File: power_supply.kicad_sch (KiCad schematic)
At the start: 29 parts, among them CON1 USB_B_Micro, CON2 Barrel_Jack_MountingPin, Q1 AO3401A, U1 AP6503, U2 CP2102N

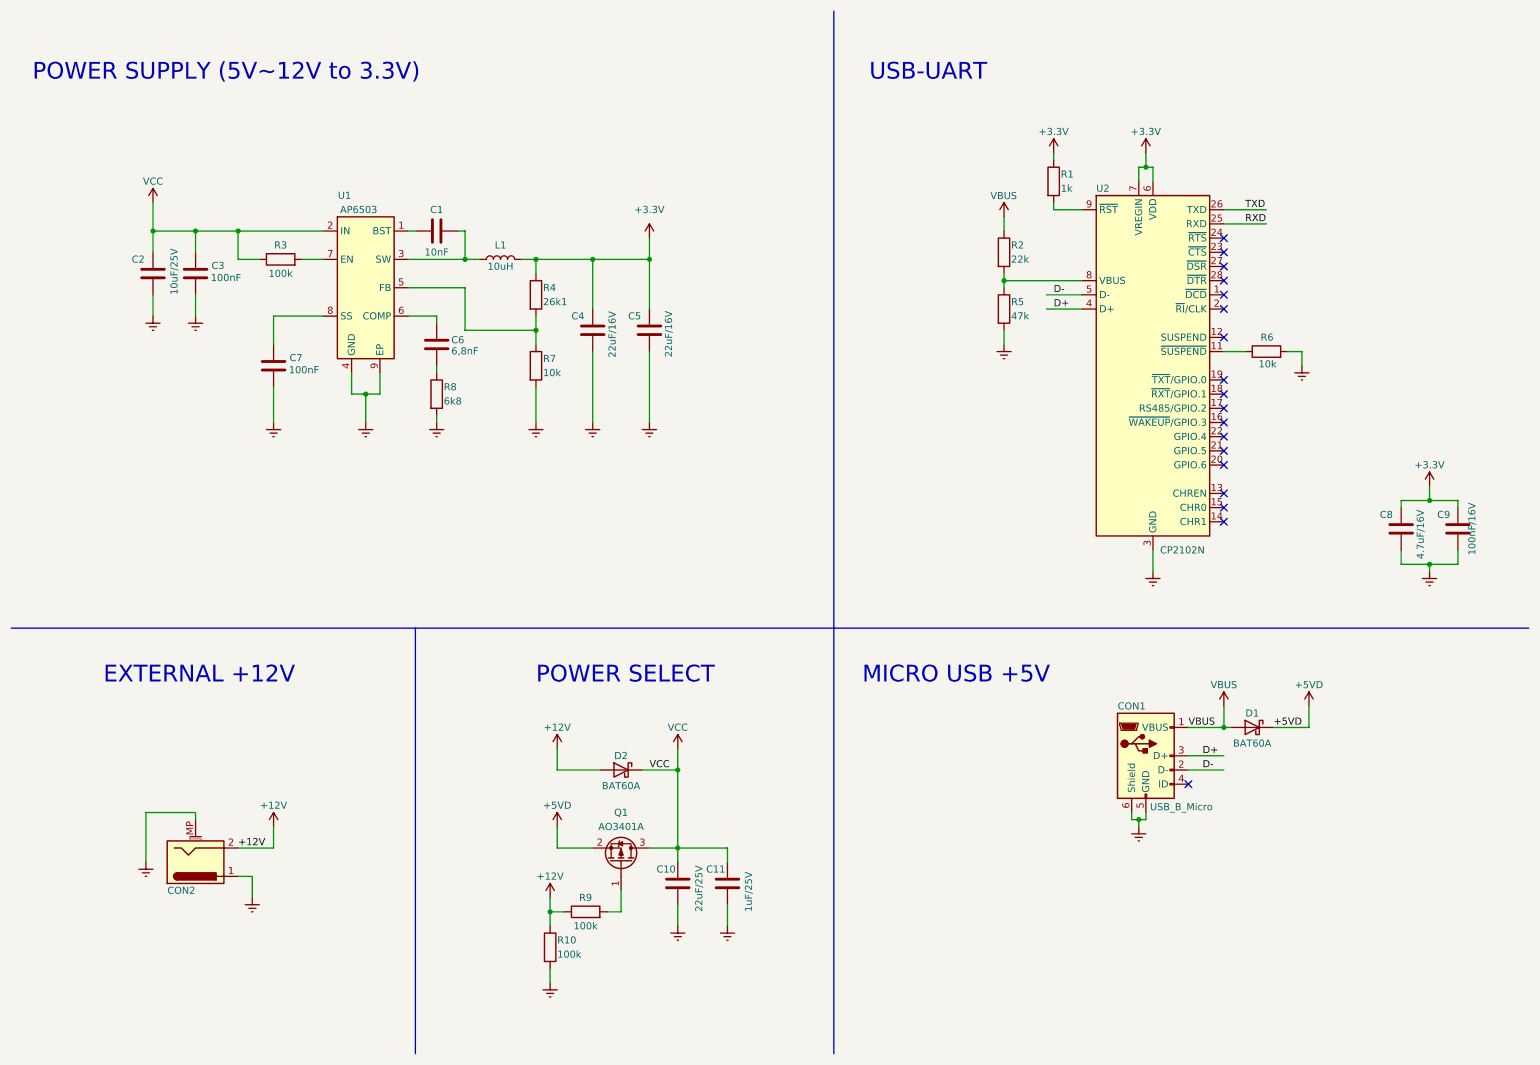
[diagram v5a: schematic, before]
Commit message: Adicionado regulador 3.3V
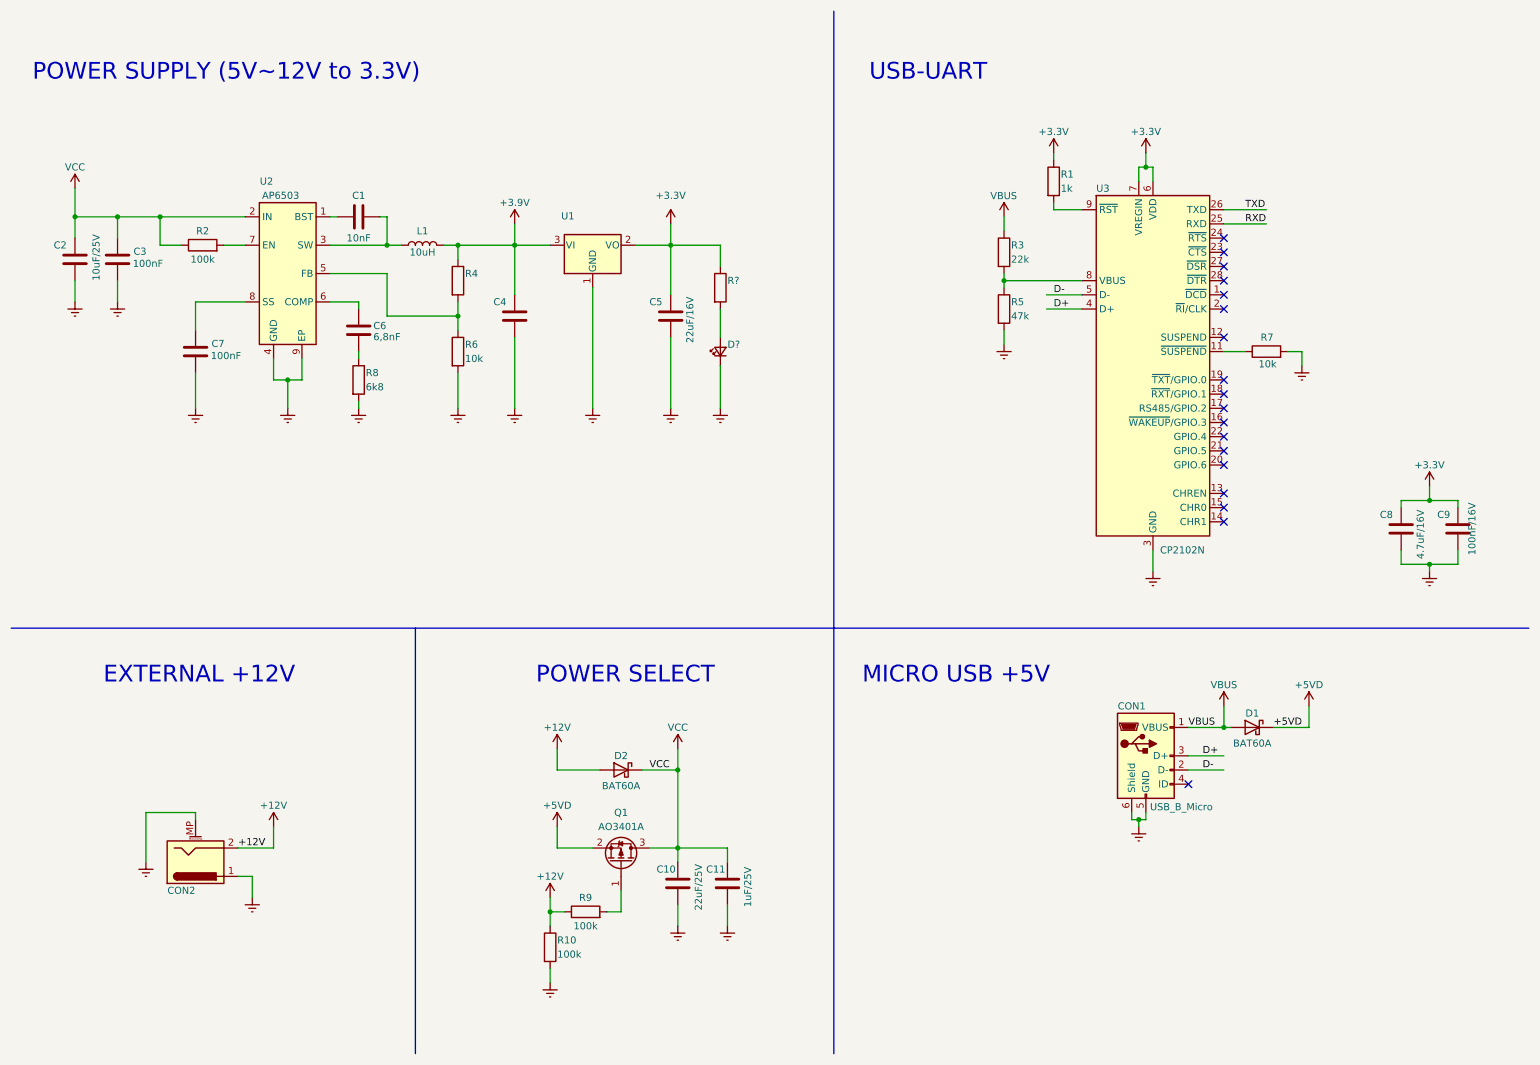
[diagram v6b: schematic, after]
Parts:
- added D?: (no value), LED_SMD:LED_0603_1608Metric_Pad1.05x0.95mm_HandSolder, symbol Device:LED_Small
- added R?: (no value), symbol Device:R
- added U1: (no value), symbol Regulator_Linear:AP1117-33
- C4: value 22uF/16V -> (none)
- R4: value 26k1 -> (none)
- renumbered R3 to R2, R2 to R3, R7 to R6, R6 to R7, U1 to U2, U2 to U3
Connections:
- net +3V3: now also R?.1, U1.2 (VO); no longer C4.1, L1.2, R4.1
- net GNDREF: now also D?.1 (K), U1.1 (GND)
- new net: D?.2 (A), R?.2
- new net: C4.1, L1.2, R4.1, U1.3 (VI)
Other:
- moved on the sheet: C1, C2, C3, C4, C5, C6, C7, L1, R2, R4, R6, R8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

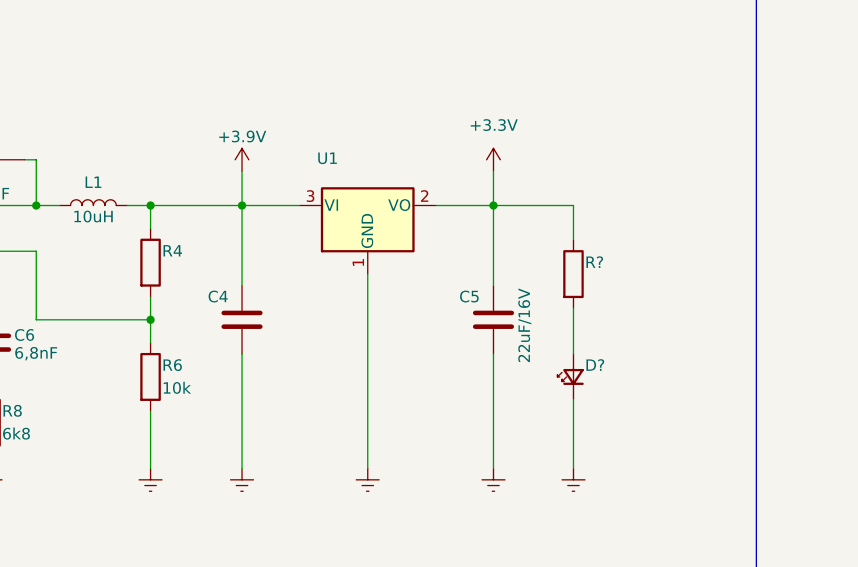
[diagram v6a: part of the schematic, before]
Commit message: Inserido o circuito do SIm Card
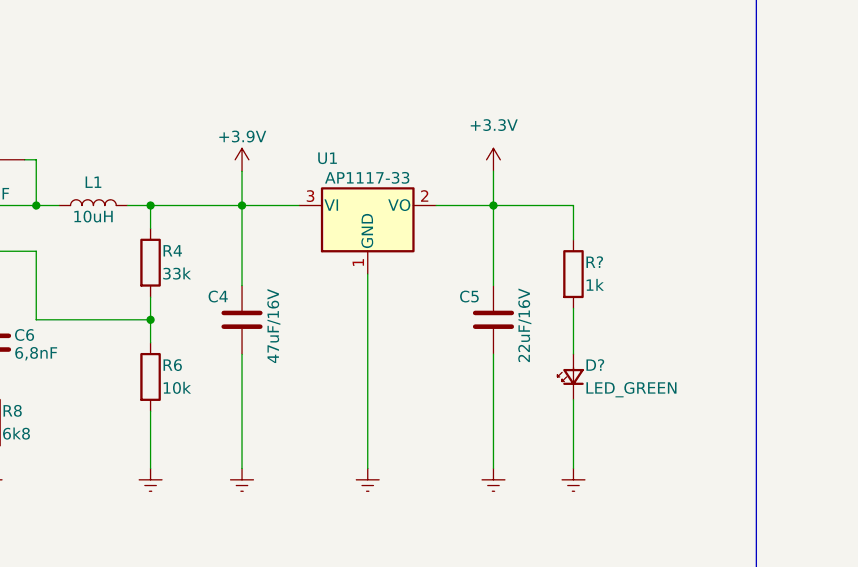
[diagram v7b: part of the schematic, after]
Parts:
- C4: value (none) -> 47uF/16V
- D?: value (none) -> LED_GREEN
- R4: value (none) -> 33k
- R?: value (none) -> 1k
- U1: value (none) -> AP1117-33; footprint (none) -> Package_TO_SOT_SMD:SOT-223-3_TabPin2
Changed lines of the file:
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@@
       (effects (font (size 1.27 1.27)) (justify left))
     )
-    (property "Value" "" (id 1) (at 140.97 62.23 0)
+    (property "Value" "1k" (id 1) (at 140.97 62.23 0)
       (effects (font (size 1.27 1.27)) (justify left))
     )
@@
       (effects (font (size 1.27 1.27)) (justify left))
     )
-    (property "Value" "" (id 1) (at 106.3842 70.9279 90)
+    (property "Value" "47uF/16V" (id 1) (at 106.3842 70.9279 90)
       (effects (font (size 1.27 1.27)) (justify left))
     )
@@
       (effects (font (size 1.27 1.27)) (justify left))
     )
-    (property "Value" "" (id 1) (at 93.98 60.96 0)
+    (property "Value" "33k" (id 1) (at 93.98 60.96 0)
       (effects (font (size 1.27 1.27)) (justify left))
     )
@@
       (effects (font (size 1.27 1.27)) (justify right))
     )
-    (property "Value" "" (id 1) (at 140.97 73.66 90)
+    (property "Value" "LED_GREEN" (id 1) (at 140.97 73.66 90)
       (effects (font (size 1.27 1.27)) (justify right))
     )
@@
     (in_bom yes) (on_board yes)
     (property "Reference" "U1" (id 0) (at 112.3788 48.1281 0))
-    (property "Value" "" (id 1) (at 116.8427 50.313 0))
-    (property "Footprint" "" (id 2) (at 116.84 48.26 0)
-      (effects (font (size 1.27 1.27)) hide)
-    )
+    (property "Value" "AP1117-33" (id 1) (at 116.8427 50.313 0))
+    (property "Footprint" "Package_TO_SOT_SMD:SOT-223-3_TabPin2" (id 2) (at 116.84 48.26 0)
+      (effects (font (size 1.27 1.27)) hide)
+    )

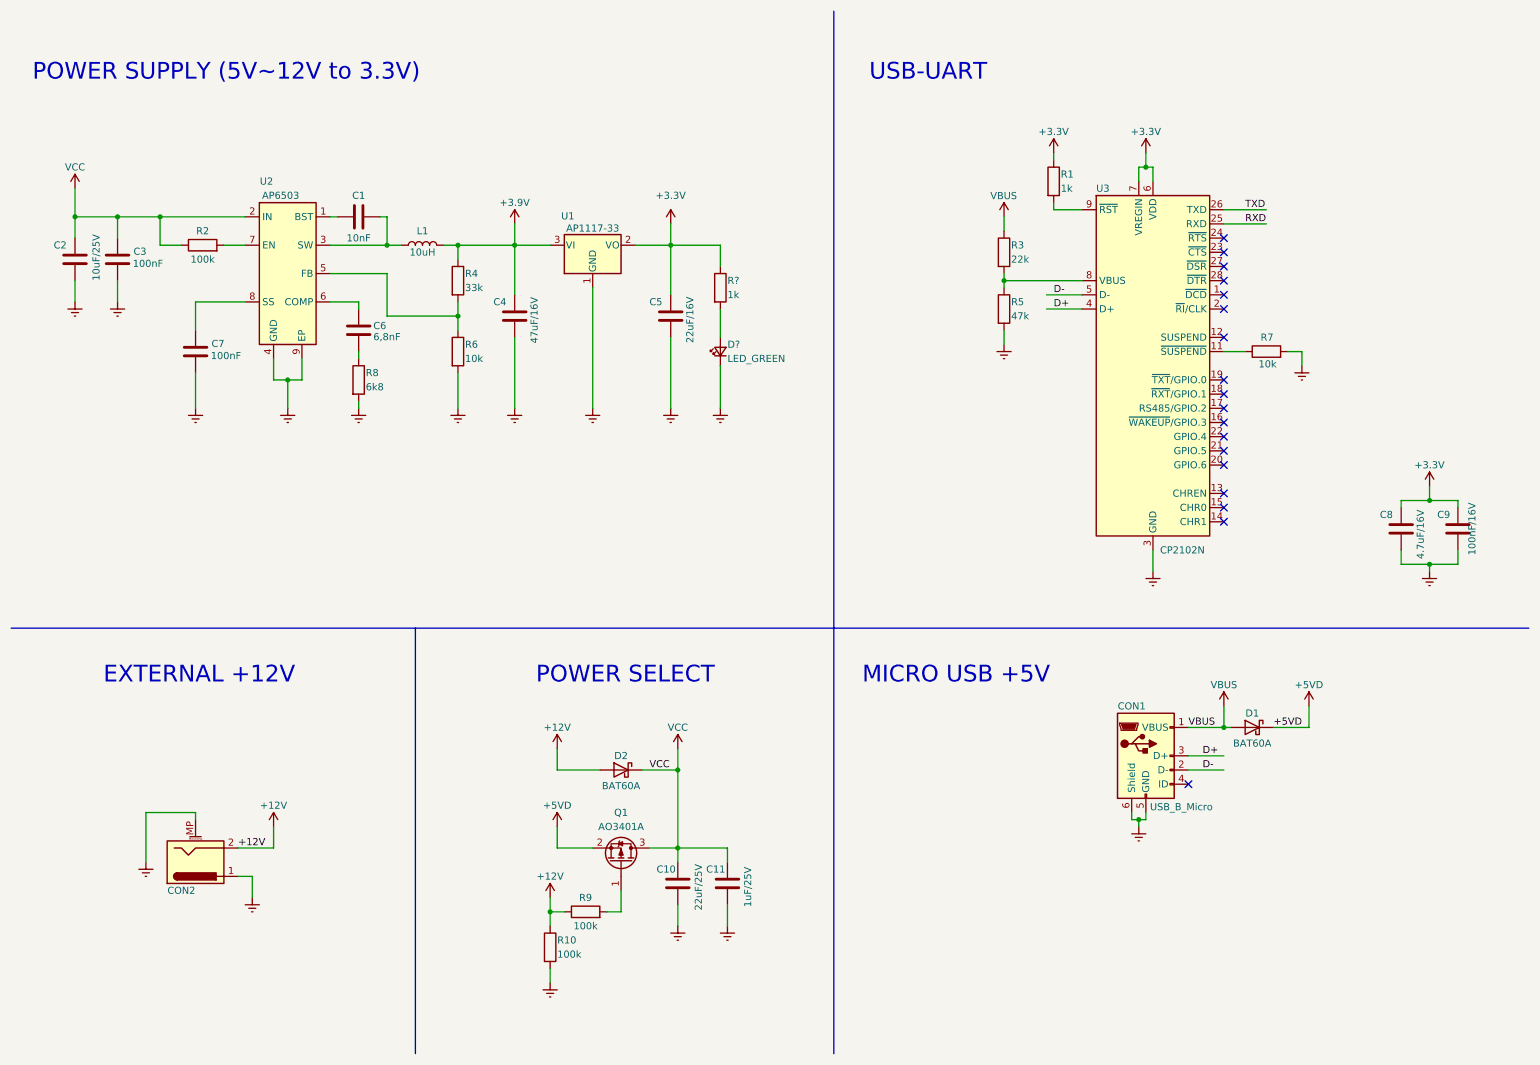
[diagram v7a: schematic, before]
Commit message: Adicionado hierarchical label
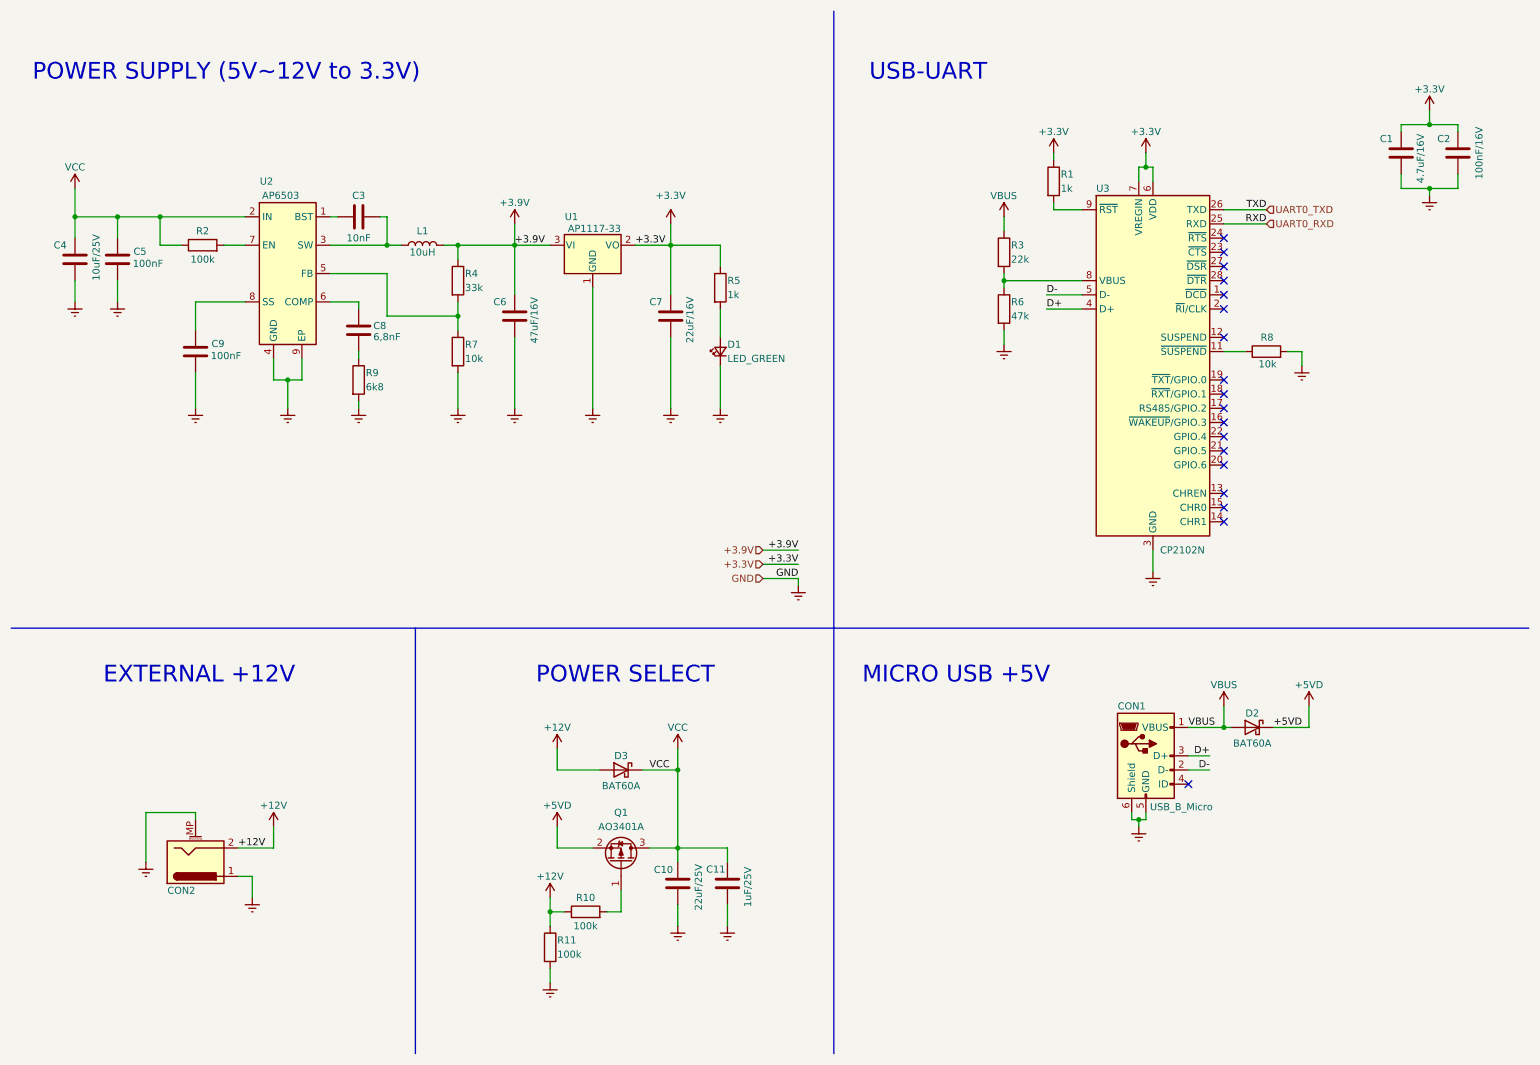
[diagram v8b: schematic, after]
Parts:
- gave numbers to parts that had none: 2
- renumbered C8 to C1, C9 to C2, C1 to C3, C2 to C4, C3 to C5, C4 to C6, C5 to C7, C6 to C8, C7 to C9, D1 to D2, D2 to D3, R9 to R10, R10 to R11, R5 to R6, R6 to R7, R7 to R8, R8 to R9
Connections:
- net +3.9V: now reaches C6.1, L1.2, R4.1, U1.3 (VI)
- net RXD renamed UART0_RXD
- net TXD renamed UART0_TXD
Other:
- moved on the sheet: C1, C2
